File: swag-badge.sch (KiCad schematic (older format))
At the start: 11 parts, among them J1 OLED_1, J2 OLED_2, J3 SAO_1, J4 SAO_2, J5 SAO_3, J6 SAO_4, J7 Lolin32, SW1 SW_Push, SW2 SW_Push, T1 Touch_slider_01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

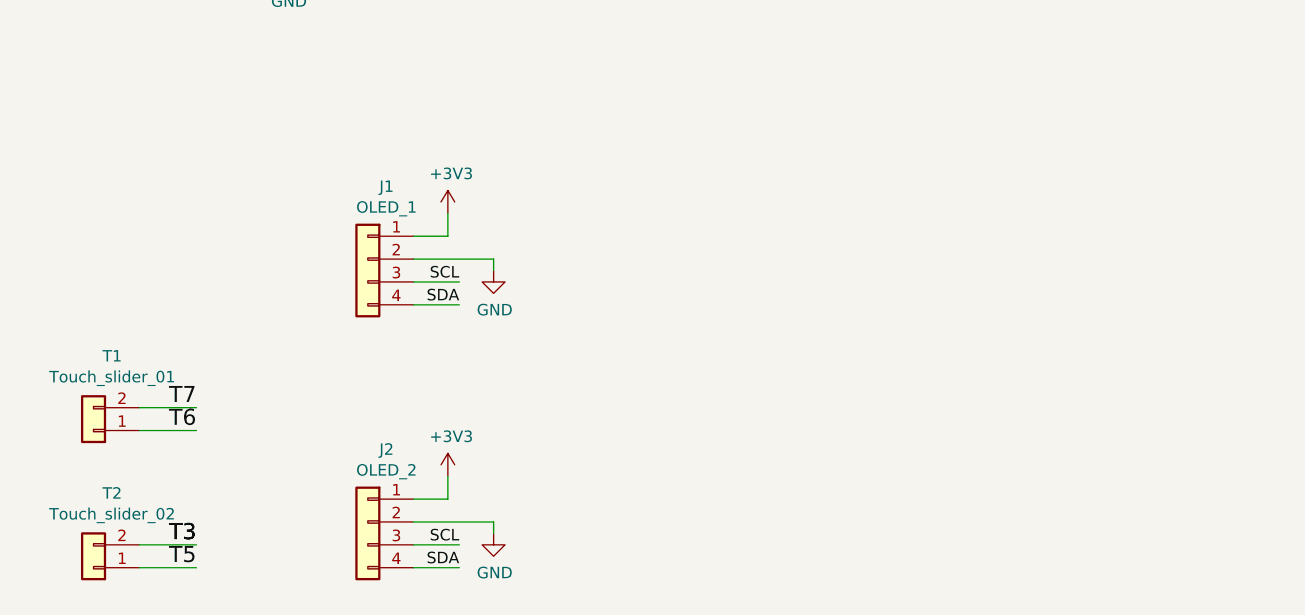
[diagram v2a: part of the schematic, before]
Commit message: Pad extensions added
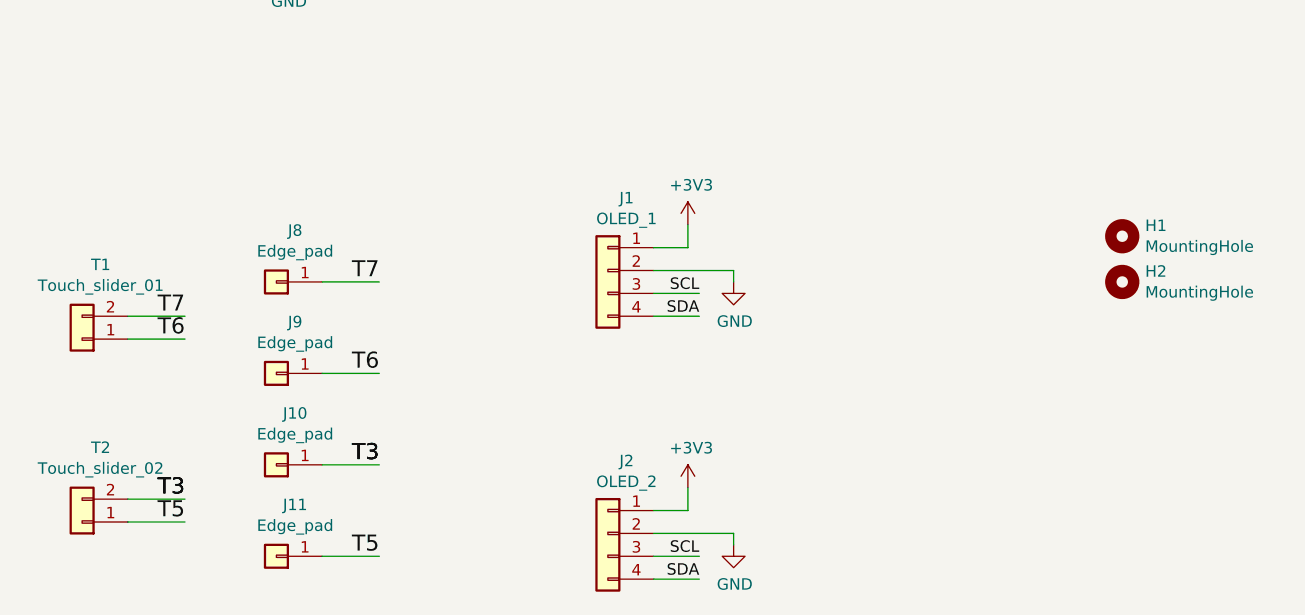
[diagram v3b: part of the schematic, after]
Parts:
- added H1, H2: MountingHole, SwagBadge:Stud_Hole_4.8mm, symbol Mechanical:MountingHole
- added J10, J11, J8, J9: Edge_pad, SwagBadge:Strain_Pad, symbol Connector_Generic:Conn_01x01
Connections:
- net GPIO12: now also J11.1 (Pin_1)
- net GPIO14: now also J9.1 (Pin_1)
- net GPIO15: now also J10.1 (Pin_1)
- net GPIO27: now also J8.1 (Pin_1)
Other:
- moved on the sheet: J1, J2, T1, T2
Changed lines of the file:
@@
 L Connector_Generic:Conn_01x04 J1
 U 1 1 5F5375FF
-P 2500 5700
-F 0 "J1" H 2418 6017 50  0000 C CNN
-F 1 "OLED_1" H 2418 5926 50  0000 C CNN
-F 2 "SwagBadge:Display_Module_128X64_I2C_SSD1306" H 2500 5700 50  0001 C CNN
-F 3 "~" H 2500 5700 50  0001 C CNN
-	1    2500 5700
+P 3550 5750
+F 0 "J1" H 3468 6067 50  0000 C CNN
+F 1 "OLED_1" H 3468 5976 50  0000 C CNN
+F 2 "SwagBadge:Display_Module_128X64_I2C_SSD1306" H 3550 5750 50  0001 C CNN
+F 3 "~" H 3550 5750 50  0001 C CNN
+	1    3550 5750
 	-1   0    0    -1
 $EndComp
@@
 L Connector_Generic:Conn_01x04 J2
 U 1 1 5F53A38D
-P 2500 6850
-F 0 "J2" H 2418 7167 50  0000 C CNN
-F 1 "OLED_2" H 2418 7076 50  0000 C CNN
-F 2 "SwagBadge:Display_Module_128X64_I2C_SSD1306" H 2500 6850 50  0001 C CNN
-F 3 "~" H 2500 6850 50  0001 C CNN
-	1    2500 6850
+P 3550 6900
+F 0 "J2" H 3468 7217 50  0000 C CNN
+F 1 "OLED_2" H 3468 7126 50  0000 C CNN
+F 2 "SwagBadge:Display_Module_128X64_I2C_SSD1306" H 3550 6900 50  0001 C CNN
+F 3 "~" H 3550 6900 50  0001 C CNN
+	1    3550 6900
 	-1   0    0    -1
 $EndComp
@@
 L power:+3V3 #PWR0106
 U 1 1 5F53F1EB
-P 2850 5500
-F 0 "#PWR0106" H 2850 5350 50  0001 C CNN
-F 1 "+3V3" H 2865 5673 50  0000 C CNN
-F 2 "" H 2850 5500 50  0001 C CNN
-F 3 "" H 2850 5500 50  0001 C CNN
-	1    2850 5500
-	1    0    0    -1
-$EndComp
-Text Label 2900 5900 2    50   ~ 0
+P 3900 5550
+F 0 "#PWR0106" H 3900 5400 50  0001 C CNN
+F 1 "+3V3" H 3915 5723 50  0000 C CNN
+F 2 "" H 3900 5550 50  0001 C CNN
+F 3 "" H 3900 5550 50  0001 C CNN
+	1    3900 5550
+	1    0    0    -1
+$EndComp
+Text Label 3950 5950 2    50   ~ 0
 SDA
-Text Label 2900 5800 2    50   ~ 0
+Text Label 3950 5850 2    50   ~ 0
 SCL
 Wire Wire Line
-	2700 5800 2900 5800
-Wire Wire Line
-	2700 5900 2900 5900
-Wire Wire Line
-	2700 5600 2850 5600
-Wire Wire Line
-	2850 5600 2850 5500
+	3750 5850 3950 5850
+Wire Wire Line
+	3750 5950 3950 5950
+Wire Wire Line
+	3750 5650 3900 5650
+Wire Wire Line
+	3900 5650 3900 5550
 $Comp
 L power:GND #PWR0107
 U 1 1 5F5403D5
-P 3050 5750
-F 0 "#PWR0107" H 3050 5500 50  0001 C CNN
-F 1 "GND" H 3055 5577 50  0000 C CNN
-F 2 "" H 3050 5750 50  0001 C CNN
-F 3 "" H 3050 5750 50  0001 C CNN
-	1    3050 5750
-	1    0    0    -1
-$EndComp
-Wire Wire Line
-	2700 5700 3050 5700
-Wire Wire Line
-	3050 5700 3050 5750
+P 4100 5800
+F 0 "#PWR0107" H 4100 5550 50  0001 C CNN
+F 1 "GND" H 4105 5627 50  0000 C CNN
+F 2 "" H 4100 5800 50  0001 C CNN
+F 3 "" H 4100 5800 50  0001 C CNN
+	1    4100 5800
+	1    0    0    -1
+$EndComp
+Wire Wire Line
+	3750 5750 4100 5750
+Wire Wire Line
+	4100 5750 4100 5800
 $Comp
 L power:+3V3 #PWR0108
 U 1 1 5F540D5F
-P 2850 6650
-F 0 "#PWR0108" H 2850 6500 50  0001 C CNN
-F 1 "+3V3" H 2865 6823 50  0000 C CNN
-F 2 "" H 2850 6650 50  0001 C CNN
-F 3 "" H 2850 6650 50  0001 C CNN
-	1    2850 6650
-	1    0    0    -1
-$EndComp
-Text Label 2900 7050 2    50   ~ 0
+P 3900 6700
+F 0 "#PWR0108" H 3900 6550 50  0001 C CNN
+F 1 "+3V3" H 3915 6873 50  0000 C CNN
+F 2 "" H 3900 6700 50  0001 C CNN
+F 3 "" H 3900 6700 50  0001 C CNN
+	1    3900 6700
+	1    0    0    -1
+$EndComp
+Text Label 3950 7100 2    50   ~ 0
 SDA
-Text Label 2900 6950 2    50   ~ 0
+Text Label 3950 7000 2    50   ~ 0
 SCL
 Wire Wire Line
-	2700 6950 2900 6950
-Wire Wire Line
-	2700 7050 2900 7050
-Wire Wire Line
-	2700 6750 2850 6750
-Wire Wire Line
-	2850 6750 2850 6650
+	3750 7000 3950 7000
+Wire Wire Line
+	3750 7100 3950 7100
+Wire Wire Line
+	3750 6800 3900 6800
+Wire Wire Line
+	3900 6800 3900 6700
 $Comp
 L power:GND #PWR0109
 U 1 1 5F540D6F
-P 3050 6900
-F 0 "#PWR0109" H 3050 6650 50  0001 C CNN
-F 1 "GND" H 3055 6727 50  0000 C CNN
-F 2 "" H 3050 6900 50  0001 C CNN
-F 3 "" H 3050 6900 50  0001 C CNN
-	1    3050 6900
-	1    0    0    -1
-$EndComp
-Wire Wire Line
-	2700 6850 3050 6850
-Wire Wire Line
-	3050 6850 3050 6900
+P 4100 6950
+F 0 "#PWR0109" H 4100 6700 50  0001 C CNN
+F 1 "GND" H 4105 6777 50  0000 C CNN
+F 2 "" H 4100 6950 50  0001 C CNN
+F 3 "" H 4100 6950 50  0001 C CNN
+	1    4100 6950
+	1    0    0    -1
+$EndComp
+Wire Wire Line
+	3750 6900 4100 6900
+Wire Wire Line
+	4100 6900 4100 6950
 $Comp
 L power:+3V3 #PWR0110
@@
 Text Label 1200 4350 0    70   ~ 0
 GPIO16
-Text Label 1750 6350 2    70   ~ 0
+Text Label 1700 5950 2    70   ~ 0
 T7
-Text Label 1750 6450 2    70   ~ 0
+Text Label 1700 6050 2    70   ~ 0
 T6
-Text Label 1750 7050 2    70   ~ 0
+Text Label 1700 6850 2    70   ~ 0
 T5
 Wire Wire Line
-	1500 6350 1750 6350
-Wire Wire Line
-	1500 6450 1750 6450
-Wire Wire Line
-	1500 7050 1750 7050
+	1450 5950 1700 5950
+Wire Wire Line
+	1450 6050 1700 6050
+Wire Wire Line
+	1450 6850 1700 6850
 $Comp
 L Connector_Generic:Conn_01x02 T1
 U 1 1 5F7E3B54
-P 1300 6450
-F 0 "T1" H 1218 6125 50  0000 C CNN
-F 1 "Touch_slider_01" H 1218 6216 50  0000 C CNN
-F 2 "SwagBadge:Touch_Slider" H 1300 6450 50  0001 C CNN
-F 3 "~" H 1300 6450 50  0001 C CNN
-	1    1300 6450
+P 1250 6050
+F 0 "T1" H 1168 5725 50  0000 C CNN
+F 1 "Touch_slider_01" H 1168 5816 50  0000 C CNN
+F 2 "SwagBadge:Touch_Slider" H 1250 6050 50  0001 C CNN
+F 3 "~" H 1250 6050 50  0001 C CNN
+	1    1250 6050
 	-1   0    0    1
 $EndComp
@@
 L Connector_Generic:Conn_01x02 T2
 U 1 1 5F7E4758
-P 1300 7050
-F 0 "T2" H 1218 6725 50  0000 C CNN
-F 1 "Touch_slider_02" H 1218 6816 50  0000 C CNN
-F 2 "SwagBadge:Touch_Slider" H 1300 7050 50  0001 C CNN
-F 3 "~" H 1300 7050 50  0001 C CNN
-	1    1300 7050
+P 1250 6850
+F 0 "T2" H 1168 6525 50  0000 C CNN
+F 1 "Touch_slider_02" H 1168 6616 50  0000 C CNN
+F 2 "SwagBadge:Touch_Slider" H 1250 6850 50  0001 C CNN
+F 3 "~" H 1250 6850 50  0001 C CNN
+	1    1250 6850
 	-1   0    0    1
 $EndComp
-Text Label 1750 6950 2    70   ~ 0
+Text Label 1700 6750 2    70   ~ 0
 T3
-Text Label 1750 6950 2    70   ~ 0
+Text Label 1700 6750 2    70   ~ 0
 T3
 Wire Wire Line
-	1500 6950 1750 6950
+	1450 6750 1700 6750
 $Comp
 L Connector_Generic:Conn_02x03_Counter_Clockwise J6
@@
 Text Label 3450 4200 0    70   ~ 0
 GPIOXX
+$Comp
+L Connector_Generic:Conn_01x01 J8
+U 1 1 5F7DFB47
+P 2100 5800
+F 0 "J8" H 2018 5575 50  0000 C CNN
+F 1 "Edge_pad" H 2018 5666 50  0000 C CNN
+F 2 "SwagBadge:Strain_Pad" H 2100 5800 50  0001 C CNN
+F 3 "~" H 2100 5800 50  0001 C CNN
+	1    2100 5800
+	-1   0    0    1
+$EndComp
+$Comp
+L Connector_Generic:Conn_01x01 J9
+U 1 1 5F7E69C4
+P 2100 6200
+F 0 "J9" H 2018 5975 50  0000 C CNN
+F 1 "Edge_pad" H 2018 6066 50  0000 C CNN
+F 2 "SwagBadge:Strain_Pad" H 2100 6200 50  0001 C CNN
+F 3 "~" H 2100 6200 50  0001 C CNN
+	1    2100 6200
+	-1   0    0    1
+$EndComp
+$Comp
+L Connector_Generic:Conn_01x01 J10
+U 1 1 5F7E9BB8
+P 2100 6600
+F 0 "J10" H 2018 6375 50  0000 C CNN
+F 1 "Edge_pad" H 2018 6466 50  0000 C CNN
+F 2 "SwagBadge:Strain_Pad" H 2100 6600 50  0001 C CNN
+F 3 "~" H 2100 6600 50  0001 C CNN
+	1    2100 6600
+	-1   0    0    1
+$EndComp
+$Comp
+L Connector_Generic:Conn_01x01 J11
+U 1 1 5F7E9BBE
+P 2100 7000
+F 0 "J11" H 2018 6775 50  0000 C CNN
+F 1 "Edge_pad" H 2018 6866 50  0000 C CNN
+F 2 "SwagBadge:Strain_Pad" H 2100 7000 50  0001 C CNN
+F 3 "~" H 2100 7000 50  0001 C CNN
+	1    2100 7000
+	-1   0    0    1
+$EndComp
+Text Label 2550 5800 2    70   ~ 0
+T7
+Text Label 2550 6200 2    70   ~ 0
+T6
+Wire Wire Line
+	2300 5800 2550 5800
+Wire Wire Line
+	2300 6200 2550 6200
+Text Label 2550 6600 2    70   ~ 0
+T3
+Text Label 2550 6600 2    70   ~ 0
+T3
+Wire Wire Line
+	2300 6600 2550 6600
+Text Label 2550 7000 2    70   ~ 0
+T5
+Wire Wire Line
+	2300 7000 2550 7000
+$Comp
+L Mechanical:MountingHole H1
+U 1 1 5F80DF84
+P 5800 5600
+F 0 "H1" H 5900 5646 50  0000 L CNN
+F 1 "MountingHole" H 5900 5555 50  0000 L CNN
+F 2 "SwagBadge:Stud_Hole_4.8mm" H 5800 5600 50  0001 C CNN
+F 3 "~" H 5800 5600 50  0001 C CNN
+	1    5800 5600
+	1    0    0    -1
+$EndComp
+$Comp
+L Mechanical:MountingHole H2
+U 1 1 5F80E9D7
+P 5800 5800
+F 0 "H2" H 5900 5846 50  0000 L CNN
+F 1 "MountingHole" H 5900 5755 50  0000 L CNN
+F 2 "SwagBadge:Stud_Hole_4.8mm" H 5800 5800 50  0001 C CNN
+F 3 "~" H 5800 5800 50  0001 C CNN
+	1    5800 5800
+	1    0    0    -1
+$EndComp
 $EndSCHEMATC

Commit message: Lanyard holes for everyone
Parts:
- added H3: MountingHole, SwagBadge:Lanyard_Hole, symbol Mechanical:MountingHole
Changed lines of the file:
@@
+	1    0    0    -1
+$EndComp
+$Comp
+L Mechanical:MountingHole H3
+U 1 1 5F7DCF4D
+P 5800 6000
+F 0 "H3" H 5900 6046 50  0000 L CNN
+F 1 "MountingHole" H 5900 5955 50  0000 L CNN
+F 2 "SwagBadge:Lanyard_Hole" H 5800 6000 50  0001 C CNN
+F 3 "~" H 5800 6000 50  0001 C CNN
+	1    5800 6000
 	1    0    0    -1
 $EndComp

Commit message: Breakouts added
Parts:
- added J12, J13: Conn_01x13, Pin_Headers:Pin_Header_Angled_1x13_Pitch2.54mm, symbol Connector_Generic:Conn_01x13
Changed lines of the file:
@@
 	1    0    0    -1
 $EndComp
+$Comp
+L Connector_Generic:Conn_01x13 J12
+U 1 1 5F7DD7C2
+P 7000 2100
+F 0 "J12" H 7080 2142 50  0000 L CNN
+F 1 "Conn_01x13" H 7080 2051 50  0000 L CNN
+F 2 "Pin_Headers:Pin_Header_Angled_1x13_Pitch2.54mm" H 7000 2100 50  0001 C CNN
+F 3 "~" H 7000 2100 50  0001 C CNN
+	1    7000 2100
+	1    0    0    -1
+$EndComp
+$Comp
+L Connector_Generic:Conn_01x13 J13
+U 1 1 5F7E62CC
+P 7800 2100
+F 0 "J13" H 7880 2142 50  0000 L CNN
+F 1 "Conn_01x13" H 7880 2051 50  0000 L CNN
+F 2 "Pin_Headers:Pin_Header_Angled_1x13_Pitch2.54mm" H 7800 2100 50  0001 C CNN
+F 3 "~" H 7800 2100 50  0001 C CNN
+	1    7800 2100
+	-1   0    0    1
+$EndComp
 $EndSCHEMATC

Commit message: Many small footprint updates
Many small updates, most importantly, SAO layout now appears to be to spec.
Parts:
- H1, H2: footprint SwagBadge:Stud_Hole_4.8mm -> SwagBadge:Lanyard_Hole_3mm
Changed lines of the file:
@@
 F 0 "H1" H 5900 5646 50  0000 L CNN
 F 1 "MountingHole" H 5900 5555 50  0000 L CNN
-F 2 "SwagBadge:Stud_Hole_4.8mm" H 5800 5600 50  0001 C CNN
+F 2 "SwagBadge:Lanyard_Hole_3mm" H 5800 5600 50  0001 C CNN
 F 3 "~" H 5800 5600 50  0001 C CNN
 	1    5800 5600
@@
 F 0 "H2" H 5900 5846 50  0000 L CNN
 F 1 "MountingHole" H 5900 5755 50  0000 L CNN
-F 2 "SwagBadge:Stud_Hole_4.8mm" H 5800 5800 50  0001 C CNN
+F 2 "SwagBadge:Lanyard_Hole_3mm" H 5800 5800 50  0001 C CNN
 F 3 "~" H 5800 5800 50  0001 C CNN
 	1    5800 5800

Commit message: LCA Logo added
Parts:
- added L1: Logo_LCA2021, SwagBadge:Logo_LCA2021_04, symbol SwagBadge:Logo_LCA2021
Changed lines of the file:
@@
 	-1   0    0    1
 $EndComp
+$Comp
+L SwagBadge:Logo_LCA2021 L1
+U 1 1 5F7ECC4B
+P 6300 5100
+F 0 "L1" H 6300 5403 50  0000 C CNN
+F 1 "Logo_LCA2021" H 6300 5312 50  0000 C CNN
+F 2 "SwagBadge:Logo_LCA2021_04" H 6300 4900 50  0001 C CNN
+F 3 "" H 6300 4900 50  0001 C CNN
+	1    6300 5100
+	1    0    0    -1
+$EndComp
 $EndSCHEMATC

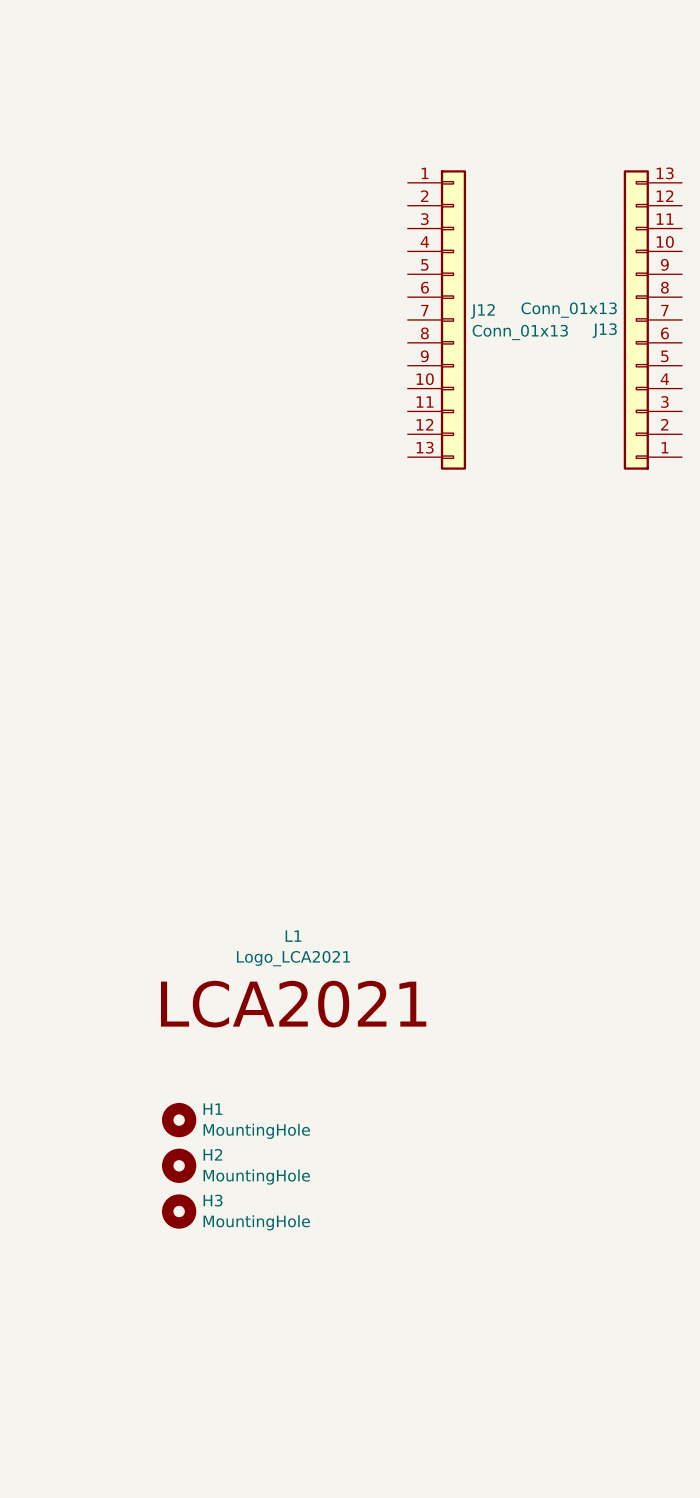
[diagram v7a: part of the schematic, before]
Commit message: Reduced breakout added to schematic
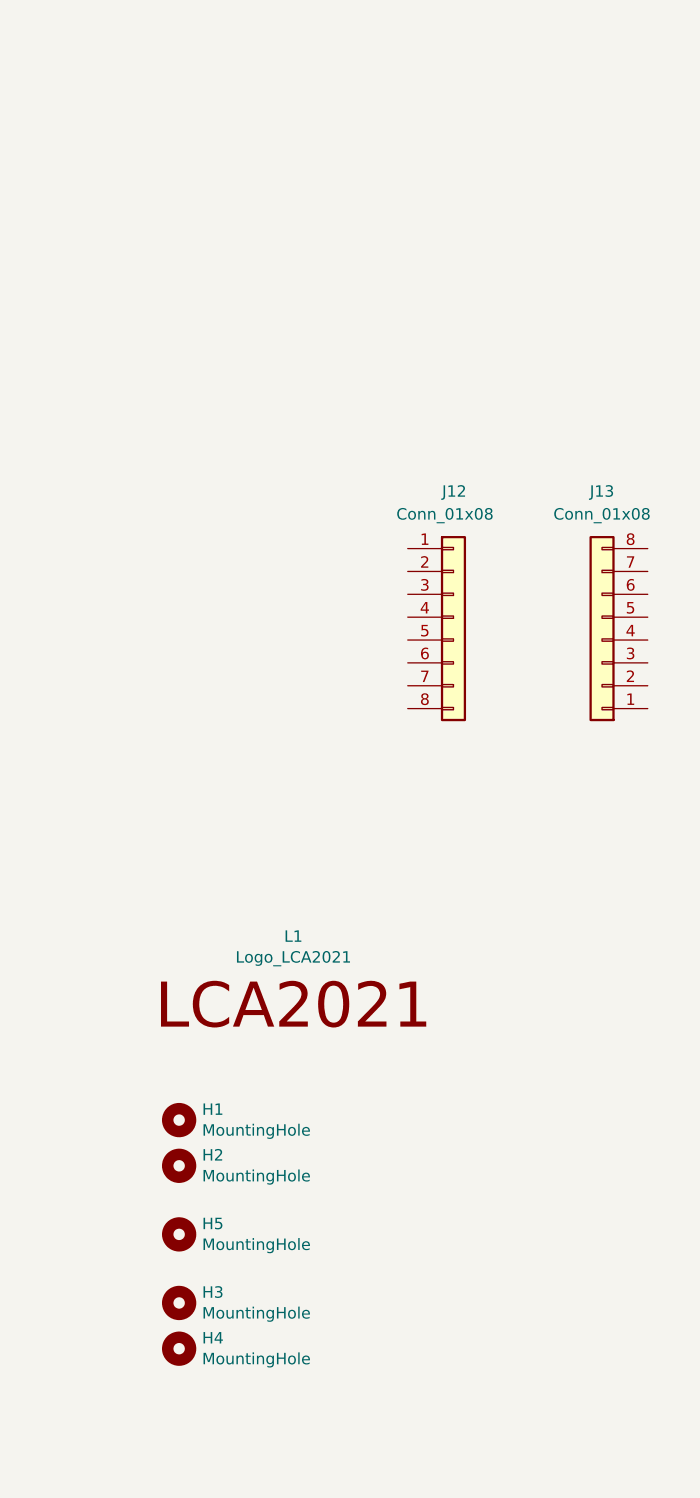
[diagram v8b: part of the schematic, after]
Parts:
- removed J12, J13: Conn_01x13, Pin_Headers:Pin_Header_Angled_1x13_Pitch2.54mm, symbol Connector_Generic:Conn_01x13
- added H3, H4: MountingHole, SwagBadge:Lanyard_Hole_3mm, symbol Mechanical:MountingHole
- added J12, J13: Conn_01x08, Pin_Headers:Pin_Header_Angled_1x08_Pitch2.54mm, symbol Connector_Generic:Conn_01x08
- renumbered H3 to H5
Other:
- moved on the sheet: H5
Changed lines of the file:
@@
 $EndComp
 $Comp
-L Mechanical:MountingHole H3
+L Mechanical:MountingHole H5
 U 1 1 5F7DCF4D
-P 5800 6000
-F 0 "H3" H 5900 6046 50  0000 L CNN
-F 1 "MountingHole" H 5900 5955 50  0000 L CNN
-F 2 "SwagBadge:Lanyard_Hole" H 5800 6000 50  0001 C CNN
-F 3 "~" H 5800 6000 50  0001 C CNN
-	1    5800 6000
+P 5800 6100
+F 0 "H5" H 5900 6146 50  0000 L CNN
+F 1 "MountingHole" H 5900 6055 50  0000 L CNN
+F 2 "SwagBadge:Lanyard_Hole" H 5800 6100 50  0001 C CNN
+F 3 "~" H 5800 6100 50  0001 C CNN
+	1    5800 6100
 	1    0    0    -1
-$EndComp
-$Comp
-L Connector_Generic:Conn_01x13 J12
-U 1 1 5F7DD7C2
-P 7000 2100
-F 0 "J12" H 7080 2142 50  0000 L CNN
-F 1 "Conn_01x13" H 7080 2051 50  0000 L CNN
-F 2 "Pin_Headers:Pin_Header_Angled_1x13_Pitch2.54mm" H 7000 2100 50  0001 C CNN
-F 3 "~" H 7000 2100 50  0001 C CNN
-	1    7000 2100
-	1    0    0    -1
-$EndComp
-$Comp
-L Connector_Generic:Conn_01x13 J13
-U 1 1 5F7E62CC
-P 7800 2100
-F 0 "J13" H 7880 2142 50  0000 L CNN
-F 1 "Conn_01x13" H 7880 2051 50  0000 L CNN
-F 2 "Pin_Headers:Pin_Header_Angled_1x13_Pitch2.54mm" H 7800 2100 50  0001 C CNN
-F 3 "~" H 7800 2100 50  0001 C CNN
-	1    7800 2100
-	-1   0    0    1
 $EndComp
 $Comp
@@
 	1    0    0    -1
 $EndComp
+$Comp
+L Mechanical:MountingHole H3
+U 1 1 5F7E99E0
+P 5800 6400
+F 0 "H3" H 5900 6446 50  0000 L CNN
+F 1 "MountingHole" H 5900 6355 50  0000 L CNN
+F 2 "SwagBadge:Lanyard_Hole_3mm" H 5800 6400 50  0001 C CNN
+F 3 "~" H 5800 6400 50  0001 C CNN
+	1    5800 6400
+	1    0    0    -1
+$EndComp
+$Comp
+L Mechanical:MountingHole H4
+U 1 1 5F7E99E6
+P 5800 6600
+F 0 "H4" H 5900 6646 50  0000 L CNN
+F 1 "MountingHole" H 5900 6555 50  0000 L CNN
+F 2 "SwagBadge:Lanyard_Hole_3mm" H 5800 6600 50  0001 C CNN
+F 3 "~" H 5800 6600 50  0001 C CNN
+	1    5800 6600
+	1    0    0    -1
+$EndComp
+$Comp
+L Connector_Generic:Conn_01x08 J12
+U 1 1 5F7FE834
+P 7000 3400
+F 0 "J12" H 6950 3950 50  0000 L CNN
+F 1 "Conn_01x08" H 6750 3850 50  0000 L CNN
+F 2 "Pin_Headers:Pin_Header_Angled_1x08_Pitch2.54mm" H 7000 3400 50  0001 C CNN
+F 3 "~" H 7000 3400 50  0001 C CNN
+	1    7000 3400
+	1    0    0    -1
+$EndComp
+$Comp
+L Connector_Generic:Conn_01x08 J13
+U 1 1 5F802AB5
+P 7650 3500
+F 0 "J13" H 7650 2850 50  0000 C CNN
+F 1 "Conn_01x08" H 7650 2950 50  0000 C CNN
+F 2 "Pin_Headers:Pin_Header_Angled_1x08_Pitch2.54mm" H 7650 3500 50  0001 C CNN
+F 3 "~" H 7650 3500 50  0001 C CNN
+	1    7650 3500
+	-1   0    0    1
+$EndComp
 $EndSCHEMATC
